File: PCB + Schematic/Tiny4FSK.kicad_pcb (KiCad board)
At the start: 4 copper layers, 35.1 x 76.3 mm, 89 parts, among them J1 Power Ext, J2 GPIO, J3 I2C, J4 USB, J5 USB Breakout, J6 SPI, J7 USBC, J8 SWD, SW1 Power Switch, SW2 RST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

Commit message: new production files
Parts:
- U4: footprint Oscillator_TCXO:ECS-327TXO-2012 -> Crystal:Crystal_SMD_3225-4Pin_3.2x2.5mm
- moved C30 2.39 mm to (141.5, 78.1)
- moved U4 1.80 mm to (143.8, 78.2)
- moved C12 0.30 mm to (143.6, 80.8)
- moved R6 0.05 mm to (145.7, 75.6)
- moved R5 0.05 mm to (145.7, 74.6)
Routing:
- net Earth: track 28.8 -> 42.8 mm, vias 147 -> 142
- net ERROR: track 28.6 -> 32.1 mm
- net +3.3V: track 71.8 -> 74.1 mm
- net MISO: track 38.6 -> 37.6 mm
- net TCXO: track 1.54 -> 2.34 mm
- net USB: track 15.3 -> 14.5 mm
- net D38: track 32.3 -> 32.8 mm

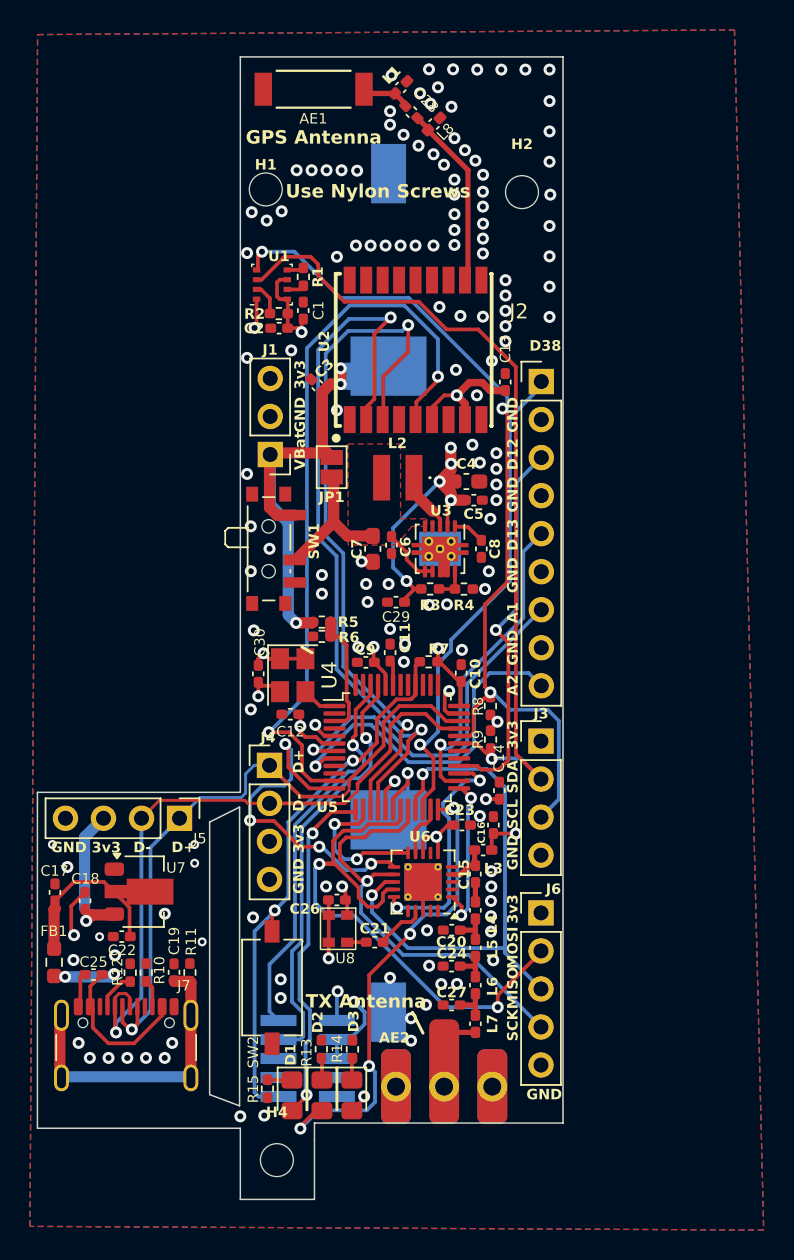
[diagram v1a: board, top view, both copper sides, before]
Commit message: add counterpoise to pcb
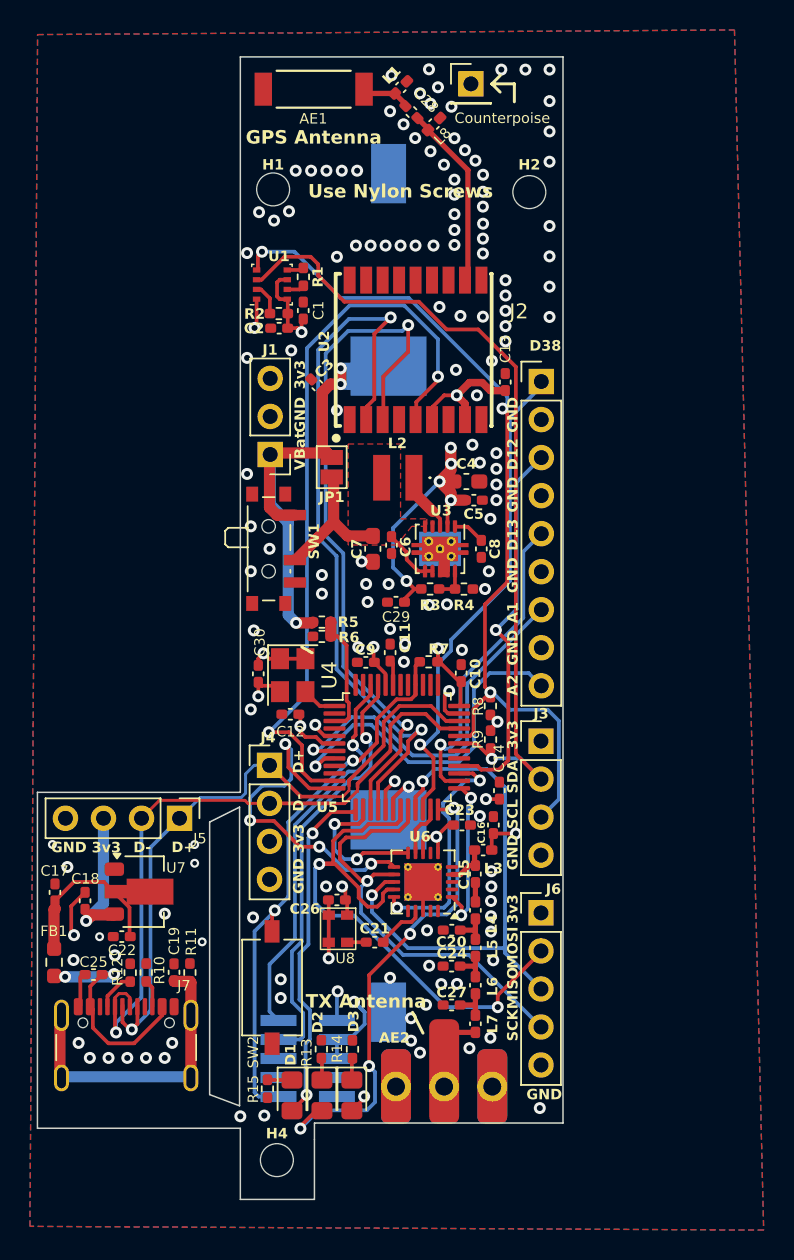
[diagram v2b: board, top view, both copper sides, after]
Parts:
- removed the G*** at (150.7, 77.4)
- removed the G*** at (150.5, 81.1)
- added G***: LOGO, LOGO, B.Cu at (150.1, 80.4)
- added G***: LOGO, LOGO, B.Cu at (150.8, 38.7)
- added J9: Counterpoise, Connector_PinHeader_2.54mm:PinHeader_1x01_P2.54mm_Vertical, F.Cu at (155.7, 38.7)
- moved G*** 1.98 mm to (150.1, 68.1)
- moved H1 0.49 mm to (142.5, 45.8)
- moved H2 0.49 mm to (159.6, 45.9)
- moved G*** 0.12 mm to (159.4, 39.3)
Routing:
- net Earth: track 42.8 -> 41.2 mm
- net +3.3V: track 74.1 -> 74.9 mm
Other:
- board text added: "09-2025"
- board text added: "Counterpoise"
- board text added: "Max Kendall W0MXX"
- board text added: "Rev. 2.2"
- board text added: "https://mpkendall.com/tiny4fsk"
- board text removed: "January 2025"
- board text removed: "Made by Max Kendall, W0MXX"
- board text removed: "Rev. 4.1"
- board text removed: "github.com/maxsrobotics/Tiny4FSK"

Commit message: new batch pcb
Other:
- board text added: "04-2026"
- board text removed: "09-2025"
- board text removed: "WayWayWay"
